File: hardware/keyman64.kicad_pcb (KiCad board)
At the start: 2 copper layers, 80 x 64.7 mm, 33 parts, among them J1 POWER, P1 COMPUTER, P2 KEYBOARD, P3 USB, P4 SERIAL, P5 CONTROL, SW1 RESET, SW2 BOOT, U1 CD74HC22106/MT8808, U2 ATMEGA1284P-PU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

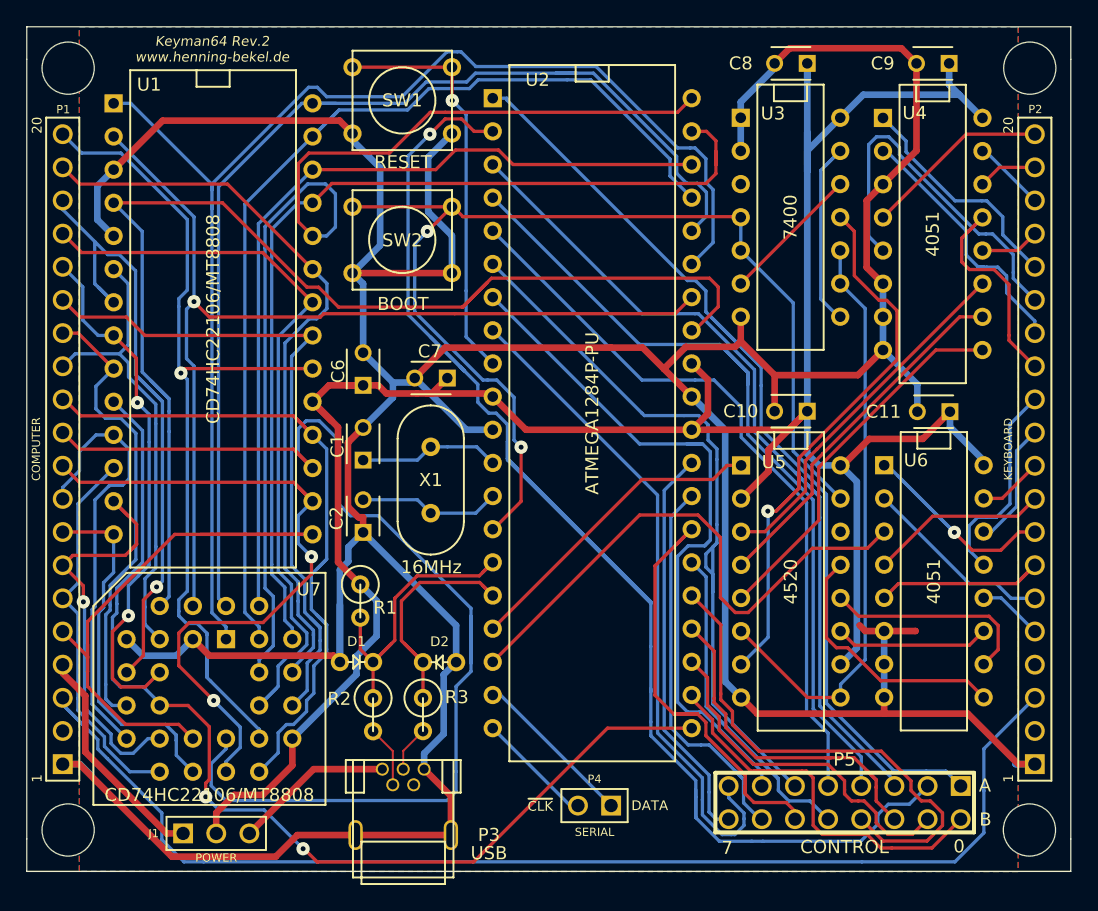
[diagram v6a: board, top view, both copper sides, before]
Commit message: Hardware: Disconnected Atmega AREF Pin, continued rerouting...
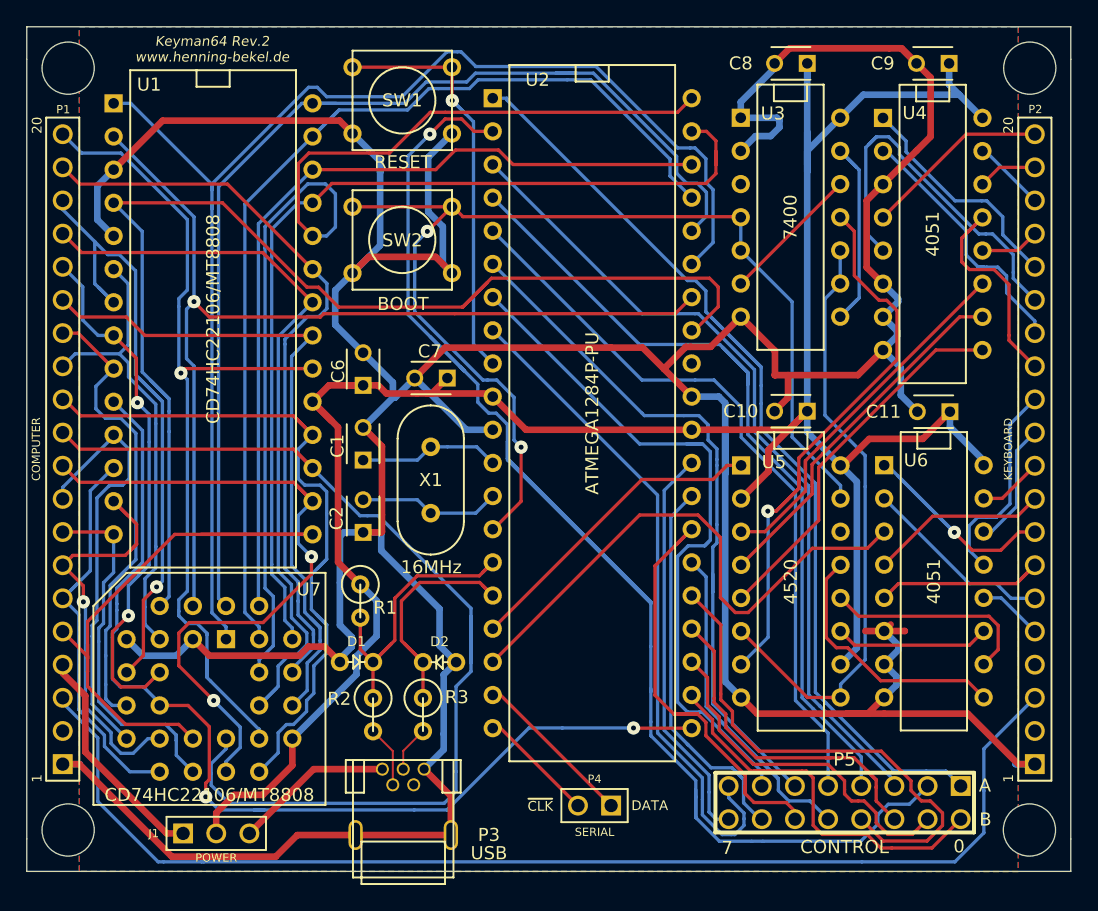
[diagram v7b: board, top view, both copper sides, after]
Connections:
- U2 pad 32: VCC -> Net-(U2-Pad32)
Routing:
- net GND: track 351.3 -> 368.2 mm
- net /B1: track 89.5 -> 80.5 mm
- net VCC: track 190.8 -> 183.8 mm
- net /UA5: track 56.6 -> 53.7 mm
- net /UA2: track 65.5 -> 62.9 mm
- net /~CPMR: track 81.2 -> 78.6 mm
- net Net-(U3-Pad13): track 15.6 -> 17.6 mm
- net /B6: track 29.3 -> 31.0 mm
- net /B0: track 53.9 -> 55.5 mm
- net /~RESET: track 31.6 -> 33.1 mm
- net /C5: track 28.1 -> 29.1 mm
- net /RCK: track 45.5 -> 46.5 mm
- net /B7: track 34.2 -> 33.4 mm
- net /CD: track 12.6 -> 12.0 mm

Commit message: Hardware: Moved USB components slightly to the right
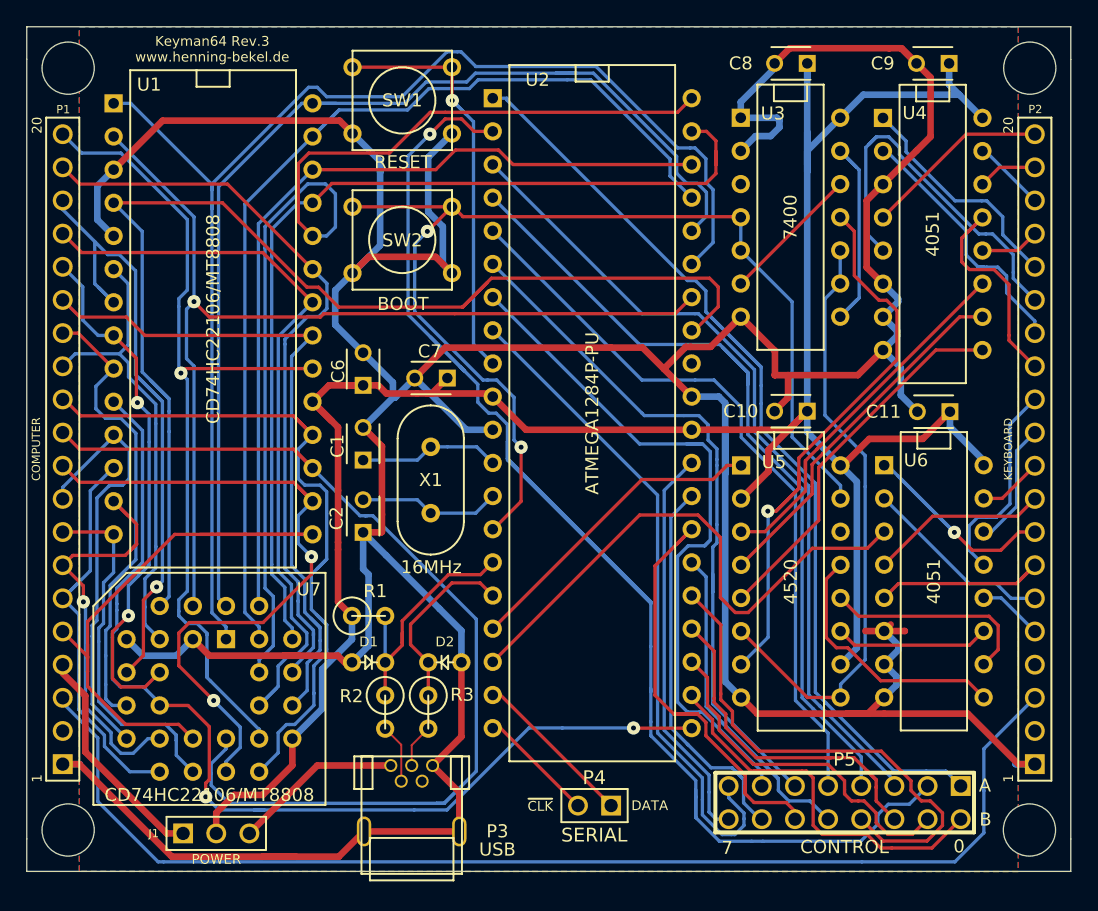
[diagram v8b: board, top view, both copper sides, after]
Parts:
- moved R1 1.31 mm to (130.8, 111.5), turned to 0 degrees
- moved R2 0.95 mm to (132.1, 118.9)
- moved D1 0.93 mm to (130.8, 115.1)
- moved P3 0.71 mm to (134.1, 128.0)
- moved R3 0.45 mm to (135.4, 118.9)
- moved D2 0.41 mm to (136.7, 115.1)
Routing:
- net Net-(D2-Pad1): track 19.7 -> 14.0 mm
- net Net-(D1-Pad1): track 23.9 -> 19.4 mm
- net VCC: track 183.8 -> 182.2 mm
- net /B1: track 80.5 -> 79.0 mm
- net GND: track 368.2 -> 369.5 mm
- net /UVCC: track 12.2 -> 13.0 mm
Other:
- net class Default: clearance 0.254 -> 0.0635
- rule trace_clearance: 0.254 -> 0.0635
- board text added: "Keyman64 Rev.3 www.henning-bekel.de"
- board text removed: "Keyman64 Rev.2 www.henning-bekel.de"
